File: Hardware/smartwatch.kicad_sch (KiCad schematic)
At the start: 52 parts, among them IC1 W25N01GVZEIG, IC2 NORA-B120-00B, IC3 LM66200DRLR, J1 Charging_Pad-, J2 Charging_Pad+, J3 DS1020-09-15VBT1A, J4 Conn_01x04_Pin, Q1 2N7002, U1 MAX17048G+T10, U11 MCP73831T-2ACI/OT, U2 RV-3028-C7_32.768KHZ_1PPM-TA-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, U3 MAX30102, U4 TPS63031DSK, U5 CAM-M8C-0, U6 AP7313-18SAG-7, U9 LIS2DE12, X2 9HT10-32.768KBZC-T

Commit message: -
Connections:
- net +3.3V: now also J3.10
- net GND: no longer J3.10
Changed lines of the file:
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@@
   (junction (at 233.0787 218.5048) (diameter 0) (color 0 0 0 0)
   )
-  (junction (at 373.8789 76.1746) (diameter 0) (color 0 0 0 0)
-  )
   (junction (at 52.6885 233.0994) (diameter 0) (color 0 0 0 0)
   )
@@
   )
   (junction (at 96.9522 169.0363) (diameter 0) (color 0 0 0 0)
+  )
+  (junction (at 372.2249 58.4089) (diameter 0) (color 0 0 0 0)
   )
   (junction (at 205.1275 133.7711) (diameter 0) (color 0 0 0 0)
@@
     (stroke (width 0) (type default))
   )
-  (wire (pts (xy 380.5547 58.4089) (xy 366.6135 58.4089))
+  (wire (pts (xy 380.5547 58.4089) (xy 372.2249 58.4089))
     (stroke (width 0) (type default))
   )
@@
     (stroke (width 0) (type default))
   )
+  (wire (pts (xy 372.2249 76.1746) (xy 372.2249 58.4089))
+    (stroke (width 0) (type default))
+  )
   (wire (pts (xy 257.9447 235.7277) (xy 263.1777 235.7277))
     (stroke (width 0) (type default))
   )
-  (wire (pts (xy 373.8789 53.3146) (xy 373.8789 76.1746))
+  (wire (pts (xy 373.8789 53.3146) (xy 373.8789 78.7146))
     (stroke (width 0) (type default))
   )
@@
     (stroke (width 0) (type default))
   )
+  (wire (pts (xy 372.2249 58.4089) (xy 366.6135 58.4089))
+    (stroke (width 0) (type default))
+  )
+  (wire (pts (xy 389.1189 76.1746) (xy 372.2249 76.1746))
+    (stroke (width 0) (type default))
+  )
   (wire (pts (xy 217.7512 62.6511) (xy 222.2427 62.6511))
     (stroke (width 0) (type default))
@@
     (stroke (width 0) (type default))
   )
-  (wire (pts (xy 373.8789 76.1746) (xy 389.1189 76.1746))
-    (stroke (width 0) (type default))
-  )
   (wire (pts (xy 102.855 207.6971) (xy 96.9204 207.6971))
     (stroke (width 0) (type default))
@@
     (stroke (width 0) (type default))
   )
-  (wire (pts (xy 373.8789 76.1746) (xy 373.8789 78.7146))
-    (stroke (width 0) (type default))
-  )

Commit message: -
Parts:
- removed J3: DS1020-09-15VBT1A, DISPLAY_CONNECTOR:FPC-SMD_P0.50-15P_LSXJ-H2.0-15P, symbol MOLEX_5022441530:5022441530
- removed Q1: 2N7002, Package_TO_SOT_SMD:SOT-23-3, symbol Device:Q_NMOS_SGD
- removed R16, R20: 4.7k, Resistor_SMD:R_0402_1005Metric, symbol Device:R
- added BT2: Battery_Cell, symbol Device:Battery_Cell
- added C11, C13, C14: 100n, Capacitor_SMD:C_0402_1005Metric, symbol Device:C
- added C12, C3: 10u, Capacitor_SMD:C_0402_1005Metric, symbol Device:C
- added J3: DF37NB-24DS-0.4V51, CONN_DF37NB-24DS-0.4V51_HIR, symbol DF37NB_24DS_0_4V_51_:DF37NB-24DS-0.4V51
- added J5: MEM2075-00-140-01-A, MEM2075_00_140_01_A:GCT_MEM2075-00-140-01-A, symbol MEM2075-00-140-01-A:MEM2075-00-140-01-A
- added MOSFET1: 2N7002, SOT-23TO-236_318-08_ONS, symbol 2N7002:2N7002
- added U7: BMI270, BMI270:XDCR_BMI270, symbol BMI270:BMI270
- added U8: LIS2MDLTR, LIS2MDLTR:PQFN50P200X200X70-12N, symbol LIS2MDLTR:LIS2MDLTR
- IC1: value W25N01GVZEIG -> W25Q256JVEIQ; footprint SON127P800X600X80-9N-D -> W25N01GVZEIG_TR:SON127P800X600X80-9N-D
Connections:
- net +1V8: now also C11.1, C13.1, C14.1, C3.1, U7.12 (CSB), U7.5 (VDDIO), U7.8 (VDD), U8.10 (VDD_IO), U8.3 (CS), U8.9 (VDD)
- net +3.3V: now also R19.2, U2.6 (VBACKUP), U2.7 (VDD), BT2.1 (+), J3.11, J3.12, J3.13, J3.14, J3.17, J3.23, J3.24; no longer IC1.8 (VCC), R21.2
- net BAT+: no longer R19.2, U2.6 (VBACKUP), U2.7 (VDD)
- net DISPLAY_CLK: now also J3.8
- net DISPLAY_CS: now also J3.9
- net DISPLAY_D/C: now also J3.5
- net DISPLAY_RESET: now also J3.10
- net DISPLAY_SDI: now also J3.6
- net FLASH_CLK: no longer IC1.6 (CLK)
- net FLASH_CS: no longer IC1.1 (~{CS})
- net FLASH_IO0: no longer IC1.5 (DI_(IO0))
- net FLASH_IO1: no longer IC1.2 (DO_(IO1))
- net FLASH_IO2: no longer IC1.3 (~{WP_(IO2)})
- net FLASH_IO3: no longer IC1.7 (~{HOLD_(IO3)}), R21.1
- net GND: now also BT2.2 (-), C11.2, C12.2, C13.2, C14.2, C3.2, J3.15, J3.16, J3.3, J3.4, MOSFET1.2 (S), U7.1 (SDO), U7.6 (GNDIO), U7.7 (GND), U8.6 (GND), U8.8 (GND); no longer IC1.4 (GND), IC1.9 (EP)
- net LEDK: now also J3.1, J3.2, MOSFET1.3 (D)
- net SCL: now also J3.20, U8.1 (SCL/SPC)
- net SDA: now also J3.19, U8.4 (SDA/SDI/SDO)
- net TP_INT: now also J3.21
- net TP_RST: now also J3.18
- net at R11.2, R3.1: now also MOSFET1.1 (G)
- new net: C12.1, U8.5 (C1)
- new net DISPLAY_SD0: J3.7
- new net INT1_BMI270: U7.4 (INT1)
- new net INT2_BMI270: U7.9 (INT2)
- new net LIS2MDLTR_INT: U8.7 (INT/DRDY/SDO)
- no-connect marks 44 -> 52
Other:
- note added: "Magnetometer"
- note added: "Step Counter"
- note added: "add micro sd card to bottom side???"
- note added: "change to 16mb flash???"
- moved on the sheet: BT1, C1, C10, C17, C18, C19, C2, C4, C5, C6, C7, C8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

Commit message: v3 schema complete
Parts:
- removed BT2: Battery_Cell, symbol Device:Battery_Cell
- removed C1: 1uF, Capacitor_SMD:C_0402_1005Metric, symbol Device:C
- removed D6: LED_GREEN, LED_SMD:LED_0402_1005Metric, symbol Device:LED
- removed J1: Charging_Pad-, power_pad:power_pad_4mm, symbol Connector:Conn_01x01_Pin
- removed J2: Charging_Pad+, power_pad:power_pad_4mm, symbol Connector:Conn_01x01_Pin
- removed J4: Conn_01x04_Pin, Connector_PinHeader_2.54mm:PinHeader_1x04_P2.54mm_Vertical, symbol Connector:Conn_01x04_Pin
- removed J5: MEM2075-00-140-01-A, MEM2075_00_140_01_A:GCT_MEM2075-00-140-01-A, symbol MEM2075-00-140-01-A:MEM2075-00-140-01-A
- removed R12, R15, R19, R21, R4, R6: 4.7k, Resistor_SMD:R_0402_1005Metric, symbol Device:R
- removed R2: 100, Resistor_SMD:R_0603_1608Metric, symbol Device:R
- removed U2: RV-3028-C7_32.768KHZ_1PPM-TA-QC, RV_3028_C7_32_768KHZ_1PPM_TA_QC:IC_RV-3028-C7_32.768KHZ_1PPM-TA-QC, symbol RV-3028-C7_32.768KHZ_1PPM-TA-QC:RV-3028-C7_32.768KHZ_1PPM-TA-QC
- removed U9: LIS2DE12, Package_LGA:LGA-12_2x2mm_P0.5mm, symbol Sensor_Motion:LIS2DE12
- added D1: LED_GREEN, LED_SMD:LED_0402_1005Metric, symbol Device:LED
- added J1, J2: Conn_01x04, Pogo_Female_4pin:Pogo_Female_4Pin, symbol Connector_Generic:Conn_01x04
- added J4: 5022441530, CONN_502244-1530_MOL, symbol MOLEX_5022441530:5022441530
- added R1: 100k, Resistor_SMD:R_0402_1005Metric, symbol Device:R
- added U2, U9: TPD2EUSB30DRTR, TPD2EUSB30DRTR:DRT0003A, symbol TPD2EUSB30DRTR:TPD2EUSB30DRTR
- BT1: footprint Capacitor_SMD:C_1812_4532Metric -> 78171-0002:78171-0002
- C12: value 10u -> 220nF
- L2: value MAMK2520H1R5M -> MBKK1608T1R5M; footprint Inductor_SMD:L_1008_2520Metric -> Inductor_SMD:L_0603_1608Metric
- R11, R13, R14, R3: footprint Resistor_SMD:R_0603_1608Metric -> Resistor_SMD:R_0402_1005Metric
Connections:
- net +3.3V: now also IC1.8 (VCC), J4.10, J4.3, J4.4, R1.2
- net DISPLAY_CLK: now also J4.7
- net DISPLAY_CS: now also J4.6
- net DISPLAY_D/C: now also J4.5
- net DISPLAY_RESET: now also J4.9
- net DISPLAY_SDI: now also J4.8
- net FLASH_CLK: now also IC1.6 (CLK)
- net FLASH_CS: now also IC1.1 (~{CS}), R1.1
- net FLASH_IO0: now also IC1.5 (DI_(IO0))
- net FLASH_IO1: now also IC1.2 (DO_(IO1))
- net FLASH_IO2: now also IC1.3 (~{WP_(IO2)})
- net FLASH_IO3: now also IC1.7 (~{HOLD_(IO3)})
- net GND: now also IC1.4 (GND), IC1.9 (EP), J1.4 (Pin_4), J2.4 (Pin_4), J4.1, J4.11, U2.3 (GND), U9.3 (GND)
- net LEDK: now also J4.2
- net SCL: now also U7.13 (SCX), J4.15
- net SDA: now also U7.14 (SDX), J4.14
- net SWDCLK: now also J2.3 (Pin_3), U9.2 (D-)
- net SWDIO: now also J2.2 (Pin_2), U9.1 (D+)
- net TP_INT: now also J4.13
- net TP_RST: now also J4.12
- net at U11.1 (STAT): now also R18.1
- net VIN_SWD: now reaches IC3.3 (VIN1), U11.4 (V_{DD})
- net VIN_SWD: now also IC2.B9 (VBUS), D1.2 (A), J1.1 (Pin_1), J2.1 (Pin_1); no longer R18.1
- net at R18.2: now also D1.1 (K)
- net USB_P: now reaches IC2.C9 (USB_DP)
- net USB_P: now also J1.3 (Pin_3), U2.1 (D+)
- net USB_N: now reaches IC2.D9 (USB_DM)
- net USB_N: now also J1.2 (Pin_2), U2.2 (D-)
- net RESET_N: no longer names the net of IC2.J3 (RESET_N)
- net SWO: no longer names the net of IC2.B3 (P0.11/TRACEDATA0/SWO/CSN)
- no-connect marks 52 -> 48
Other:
- note added: "Accelerometer & Gyroscope"
- note added: "ESD Protection"
- note added: "NORA B126 Module"
- note added: "SWD Pogo Connector"
- note added: "USB Pogo Connector"
- note removed: "Accelometer"
- note removed: "MCU"
- note removed: "RTC"
- note removed: "Step Counter"
- note removed: "add micro sd card to bottom side???"
- note removed: "change to 16mb flash???"
- moved on the sheet: BT1, C10, C11, C12, C13, C14, C17, C18, C19, C2, C3, C4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

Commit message: -
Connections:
- net +1V8: now also R13.2, R14.2
- net +3.3V: no longer R13.2, R14.2
- net BAT_INT: now reaches U1.5 (*ALRT)
- net BAT_INT: now also IC2.G4 (P1.04)
- no-connect marks 48 -> 46
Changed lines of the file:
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@@
   (no_connect (at 118.9167 313.5406))
   (no_connect (at 112.4848 149.347))
-  (no_connect (at 66.0589 240.4074))
   (no_connect (at 270.192 101.8567))
   (no_connect (at 270.192 129.7967))
@@
   (no_connect (at 331.152 114.5567))
   (no_connect (at 331.152 96.7767))
-  (no_connect (at 331.152 101.8567))
   (no_connect (at 331.152 134.8767))
   (no_connect (at 270.192 124.7167))
@@
     (stroke (width 0) (type default))
   )
+  (wire (pts (xy 331.7374 101.8567) (xy 331.152 101.8567))
+    (stroke (width 0) (type default))
+  )
   (wire (pts (xy 74.6848 333.8757) (xy 78.2767 333.8757))
     (stroke (width 0) (type default))
@@
     (stroke (width 0) (type default))
   )
+  (wire (pts (xy 332.8518 101.8685) (xy 331.7374 101.8685))
+    (stroke (width 0) (type default))
+  )
   (wire (pts (xy 462.8764 164.0441) (xy 465.6566 164.0441))
     (stroke (width 0) (type default))
@@
     (stroke (width 0) (type default))
   )
+  (wire (pts (xy 331.7374 101.8685) (xy 331.7374 101.8567))
+    (stroke (width 0) (type default))
+  )
   (wire (pts (xy 253.2533 104.3967) (xy 270.192 104.3967))
     (stroke (width 0) (type default))
@@
     (fill (type none))
   )
-  (rectangle (start 34.9784 275.2697) (end 158.5445 369.8847)
+  (rectangle (start 35.814 275.2697) (end 158.5445 369.8847)
     (stroke (width 0) (type dash))
     (fill (type none))
@@
     (effects (font (size 1.27 1.27)) (justify right bottom))
   )
+  (label "BAT_INT" (at 332.8518 101.8685 0) (fields_autoplaced)
+    (effects (font (size 1.27 1.27)) (justify left bottom))
+  )
   (label "FLASH_CLK" (at 511.3631 269.6915 180) (fields_autoplaced)
     (effects (font (size 1.27 1.27)) (justify right bottom))
@@
     (effects (font (size 1.27 1.27)) (justify left bottom))
   )
+  (label "BAT_INT" (at 66.0589 240.4074 180) (fields_autoplaced)
+    (effects (font (size 1.27 1.27)) (justify right bottom))
+  )
   (label "BAT+" (at 121.771 144.2733 0) (fields_autoplaced)
     (effects (font (size 1.27 1.27)) (justify left bottom))
@@
     )
   )
-  (symbol (lib_id "power:+3.3V") (at 346.0682 116.4272 270) (unit 1)
-    (in_bom yes) (on_board yes) (dnp no)
-    (property "Reference" "#PWR042" (at 342.2582 116.4272 0)
-      (effects (font (size 1.27 1.27)) hide)
-    )
-    (property "Value" "+3.3V" (at 351.9138 116.5584 90)
-      (effects (font (size 1.27 1.27)))
-    )
-    (property "Footprint" "" (at 346.0682 116.4272 0)
-      (effects (font (size 1.27 1.27)) hide)
-    )
-    (property "Datasheet" "" (at 346.0682 116.4272 0)
-      (effects (font (size 1.27 1.27)) hide)
-    )
-    (pin "1")
-    (instances
-      (project "smartwatch"
-        (path "/66aaca1a-81b1-4743-8182-fb4c70cf8a2a"
-          (reference "#PWR042") (unit 1)
-        )
-      )
-    )
-  )
   (symbol (lib_id "Device:C") (at 132.1101 250.9067 0) (unit 1)
     (in_bom yes) (on_board yes) (dnp no)
@@
     )
   )
+  (symbol (lib_id "power:+1V8") (at 346.492 99.898 270) (unit 1)
+    (in_bom yes) (on_board yes) (dnp no)
+    (property "Reference" "#PWR044" (at 342.682 99.898 0)
+      (effects (font (size 1.27 1.27)) hide)
+    )
+    (property "Value" "+1V8" (at 352.4439 99.971 90)
+      (effects (font (size 1.27 1.27)))
+    )
+    (property "Footprint" "" (at 346.492 99.898 0)
+      (effects (font (size 1.27 1.27)) hide)
+    )
+    (property "Datasheet" "" (at 346.492 99.898 0)
+      (effects (font (size 1.27 1.27)) hide)
+    )
+    (pin "1")
+    (instances
+      (project "smartwatch"
+        (path "/66aaca1a-81b1-4743-8182-fb4c70cf8a2a"
+          (reference "#PWR044") (unit 1)
+        )
+      )
+    )
+  )
   (symbol (lib_id "Device:C") (at 435.6728 330.8014 0) (unit 1)
     (in_bom yes) (on_board yes) (dnp no) (fields_autoplaced)
@@
     )
   )
-  (symbol (lib_id "power:+3.3V") (at 346.492 99.898 270) (unit 1)
-    (in_bom yes) (on_board yes) (dnp no)
-    (property "Reference" "#PWR041" (at 342.682 99.898 0)
-      (effects (font (size 1.27 1.27)) hide)
-    )
-    (property "Value" "+3.3V" (at 352.3376 100.0292 90)
-      (effects (font (size 1.27 1.27)))
-    )
-    (property "Footprint" "" (at 346.492 99.898 0)
-      (effects (font (size 1.27 1.27)) hide)
-    )
-    (property "Datasheet" "" (at 346.492 99.898 0)
-      (effects (font (size 1.27 1.27)) hide)
-    )
-    (pin "1")
-    (instances
-      (project "smartwatch"
-        (path "/66aaca1a-81b1-4743-8182-fb4c70cf8a2a"
-          (reference "#PWR041") (unit 1)
-        )
-      )
-    )
-  )
   (symbol (lib_id "LM66200DRLR:LM66200DRLR") (at 79.4648 141.727 0) (unit 1)
     (in_bom yes) (on_board yes) (dnp no) (fields_autoplaced)
@@
         )
       )
+    )
+  )
+  (symbol (lib_id "power:+1V8") (at 346.0682 116.4272 270) (unit 1)
+    (in_bom yes) (on_board yes) (dnp no)
+    (property "Reference" "#PWR047" (at 342.2582 116.4272 0)
+      (effects (font (size 1.27 1.27)) hide)
+    )
+    (property "Value" "+1V8" (at 351.6045 116.5843 90)
+      (effects (font (size 1.27 1.27)))
+    )
+    (property "Footprint" "" (at 346.0682 116.4272 0)
+      (effects (font (size 1.27 1.27)) hide)
+    )
+    (property "Datasheet" "" (at 346.0682 116.4272 0)
+      (effects (font (size 1.27 1.27)) hide)
+    )
+    (pin "1")
+    (instances
+      (project "smartwatch"
+        (path "/66aaca1a-81b1-4743-8182-fb4c70cf8a2a"
+          (reference "#PWR047") (unit 1)
+        )
+      )

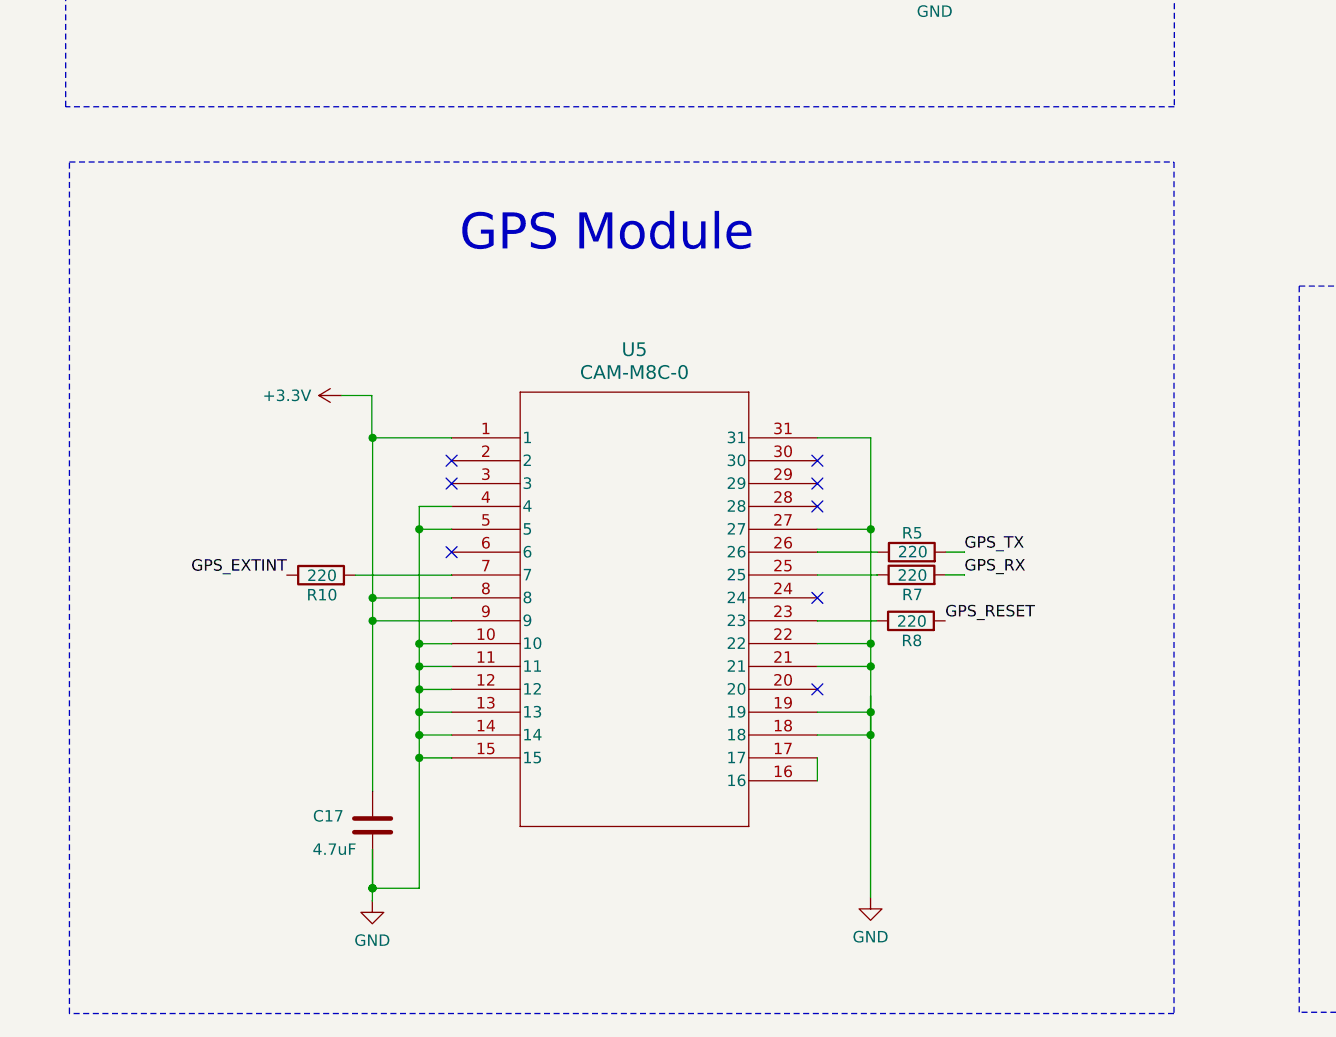
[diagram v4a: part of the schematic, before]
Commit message: changed gps moduleto l96
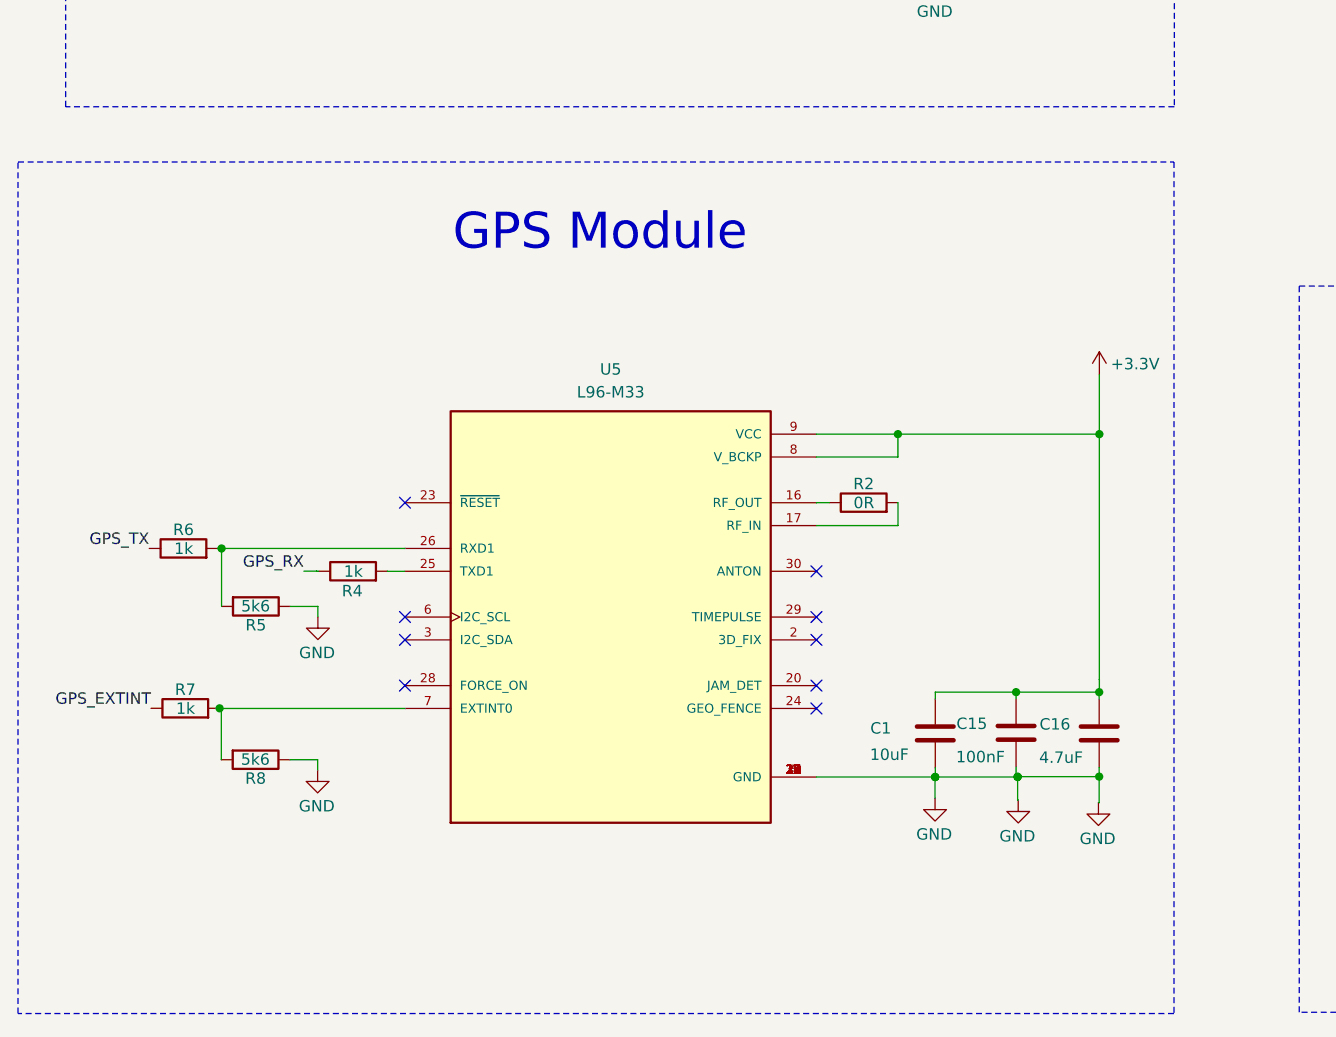
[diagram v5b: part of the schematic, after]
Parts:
- removed C17: 4.7uF, Capacitor_SMD:C_0402_1005Metric, symbol Device:C
- removed R10: 220, Resistor_SMD:R_0402_1005Metric, symbol Device:R
- removed U5: CAM-M8C-0, QFN_M8C-0_UBL, symbol CAM-M8C:CAM-M8C-0
- added C1: 10uF, Capacitor_SMD:C_0402_1005Metric, symbol Device:C
- added C15: 100nF, Capacitor_SMD:C_0402_1005Metric, symbol Device:C
- added C16: 4.7uF, Capacitor_SMD:C_0402_1005Metric, symbol Device:C
- added R2: 0R, Resistor_SMD:R_0402_1005Metric, symbol Device:R
- added R4, R6: 1k, Resistor_SMD:R_0402_1005Metric, symbol Device:R
- added U5: L96-M33, L96-M33:XCVR_L96-M33, symbol L96-M33:L96-M33
- R5, R8: value 220 -> 5k6
- R7: value 220 -> 1k
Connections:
- net +3.3V: now also C1.1, C15.1, C16.1, U5.8 (V_BCKP), U5.9 (VCC)
- net GND: now also R5.1, R8.1, C1.2, C15.2, C16.2, U5.10 (GND), U5.11 (GND), U5.12 (GND), U5.13 (GND), U5.14 (GND), U5.15 (GND), U5.18 (GND), U5.19 (GND), U5.21 (GND), U5.22 (GND), U5.27 (GND), U5.31 (GND), U5.4 (GND), U5.5 (GND)
- net GPS_EXTINT: now also R7.1
- net GPS_RESET: no longer R8.2
- net GPS_RX: now also R4.1; no longer R7.2
- net GPS_TX: now also R6.1; no longer R5.2
- new net: R7.2, R8.2, U5.7 (EXTINT0)
- new net: R4.2, U5.25 (TXD1)
- new net: R5.2, R6.2, U5.26 (RXD1)
- new net: R2.1, U5.16 (RF_OUT)
- new net: R2.2, U5.17 (RF_IN)
- no-connect marks 46 -> 47

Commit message: added rtc
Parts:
- added BT2: 2994TR, 2994TR:BAT_2994TR, symbol 2994TR:2994TR
- added U10: RV-3028-C7_32.768KHZ_1PPM-TA-QC, RV-3028-C7_32.768KHZ_1PPM-TA-QC:IC_RV-3028-C7_32.768KHZ_1PPM-TA-QC, symbol RV-3028-C7_32.768KHZ_1PPM-TA-QC:RV-3028-C7_32.768KHZ_1PPM-TA-QC
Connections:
- net GPS_RESET is gone; now on net GPS_EXTINT: IC2.A2 (P0.12/TRACECLK/DCX)
- net +3.3V: now also U10.7 (VDD); no longer U5.8 (V_BCKP)
- net GND: now also BT2.N, U10.5 (VSS)
- net INT1_BMI270: now also IC2.J4 (N/C_3)
- net INT2_BMI270: now also IC2.J5 (N/C_4)
- net LIS2MDLTR_INT: now also IC2.J3 (RESET_N)
- net RTC_CLK: now also U10.1 (CLKOUT)
- net RTC_EVI: now also U10.8 (EVI)
- net RTC_INT: now also U10.2 (~{INT})
- net SCL: now also U10.3 (SCL)
- net SDA: now also U10.4 (SDA)
- new net RTC Battery: BT2.P1, U5.8 (V_BCKP)
- no-connect marks 47 -> 44
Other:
- note added: "RTC"
- note added: "RTC Battery"
